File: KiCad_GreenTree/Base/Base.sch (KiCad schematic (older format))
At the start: 21 parts, among them Q1 BCX56, Q2 BCX56, Q3 BCX56, Q4 BCX56, SW1 SW_DPDT_x2, U1 NE555D, U2 NE555D, U3 74HC04

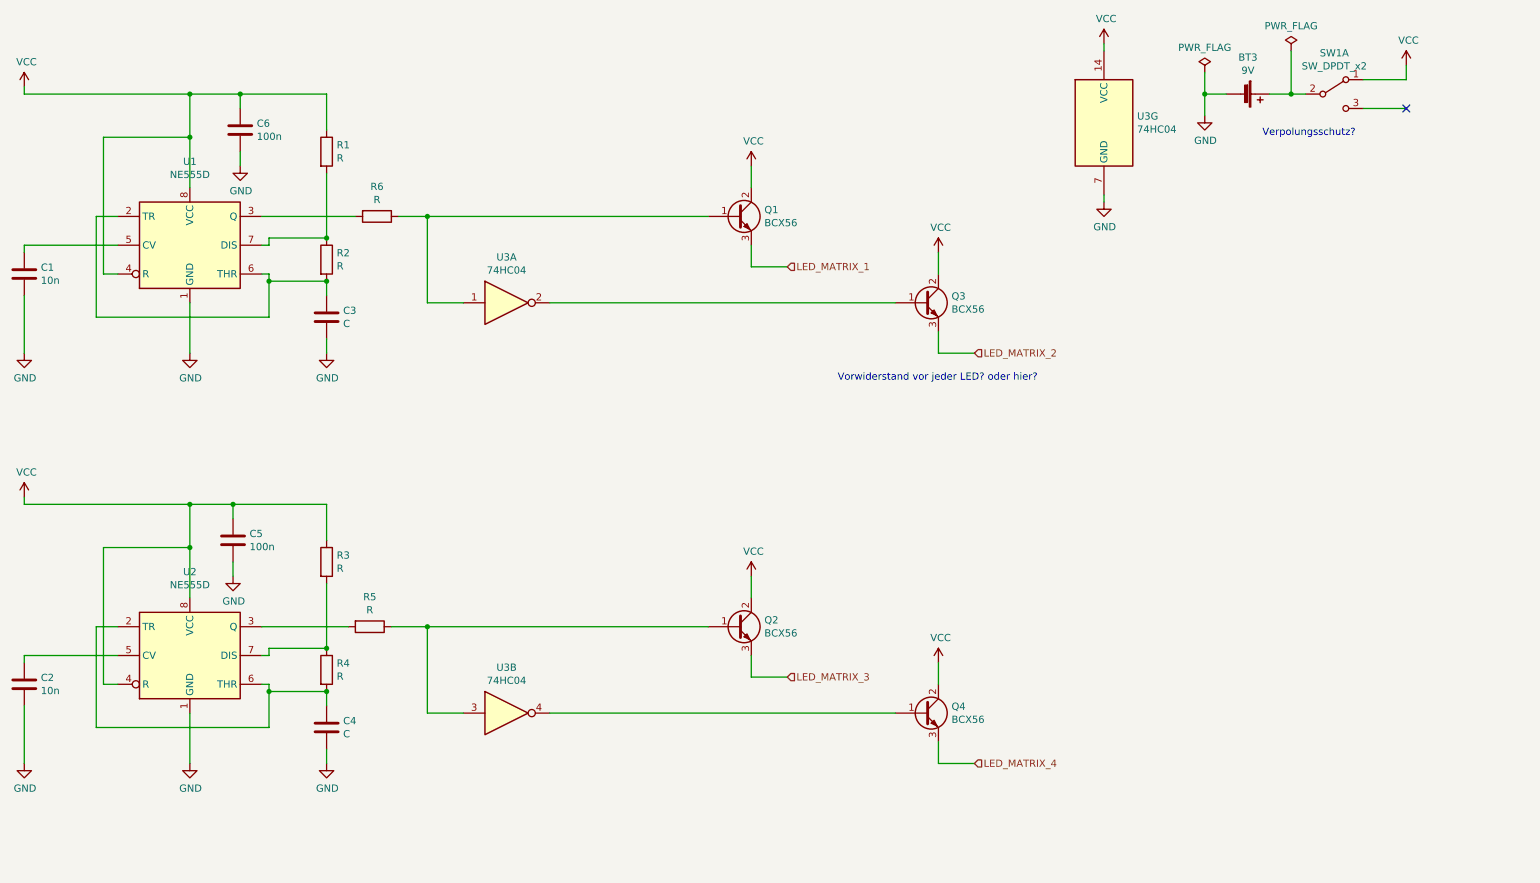
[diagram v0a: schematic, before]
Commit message: ordentlicher Schaltplan
NO DRC errors anymore
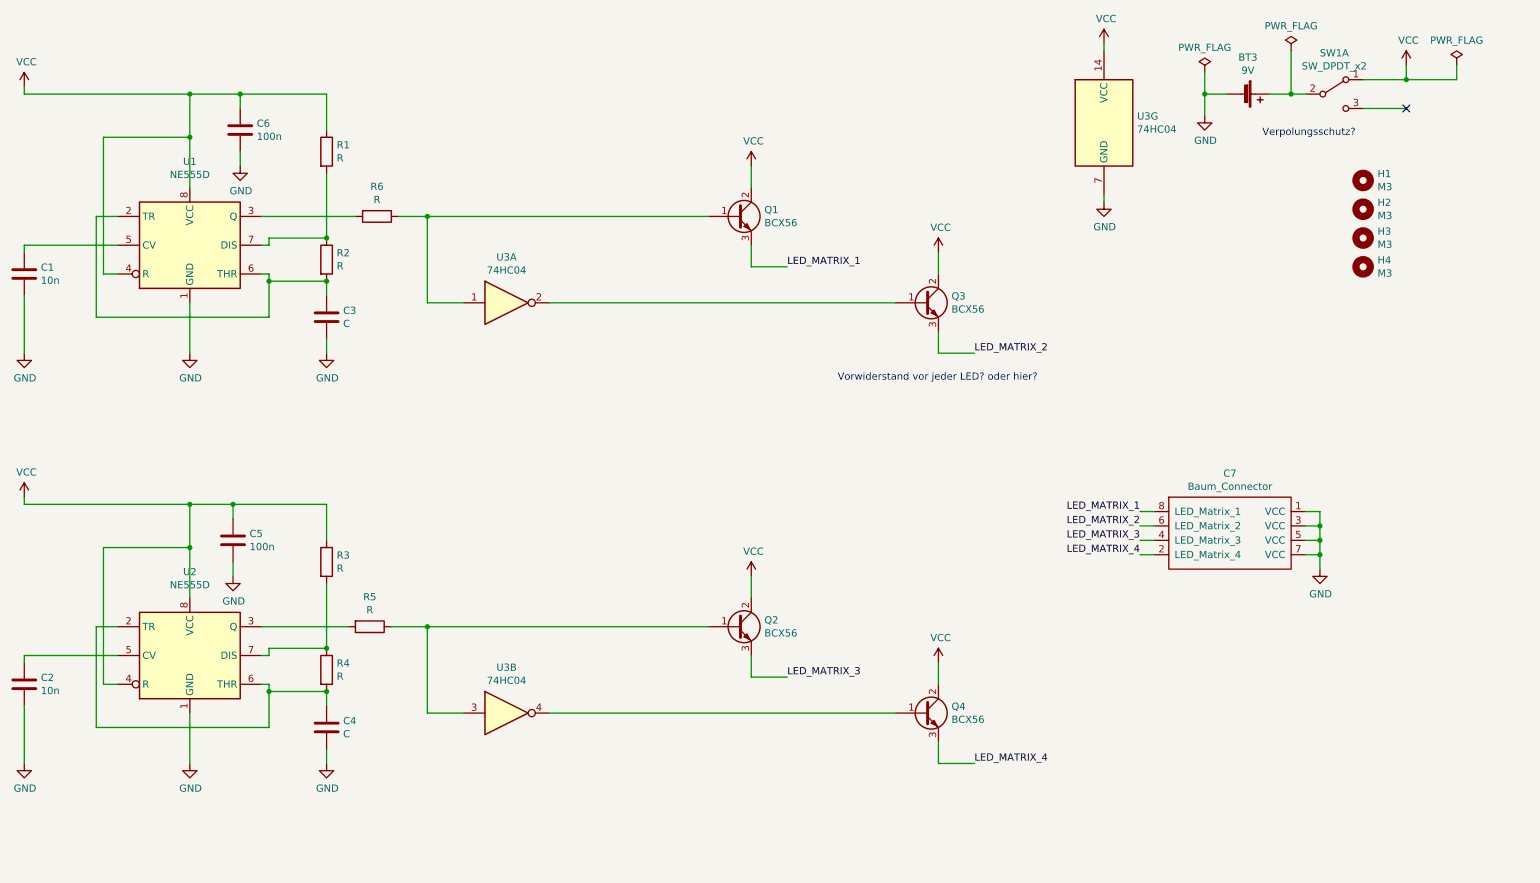
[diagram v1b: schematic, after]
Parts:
- added C7: Baum_Connector, Bib:Verbindung_Basis, symbol New_Library:Baum_Connector
- added H1, H2, H3, H4: M3, MountingHole:MountingHole_3.2mm_M3, symbol Mechanical:MountingHole
- U3: footprint (none) -> Package_SO:SOIC-14W_7.5x9mm_P1.27mm
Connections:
- net GND: now also C7.1 (VCC), C7.3 (VCC), C7.5 (VCC), C7.7 (VCC)
- net LED_MATRIX_1: now also C7.8 (LED_Matrix_1)
- net LED_MATRIX_2: now also C7.6 (LED_Matrix_2)
- net LED_MATRIX_3: now also C7.4 (LED_Matrix_3)
- net LED_MATRIX_4: now also C7.2 (LED_Matrix_4)
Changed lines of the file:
@@
 Wire Wire Line
 	2950 1050 2950 1300
-Connection ~ 2000 1050
 Wire Wire Line
 	2950 2450 2950 2350
@@
 $EndComp
 Wire Wire Line
-	850  1000 850  1050
-Wire Wire Line
 	1500 1900 1350 1900
 Wire Wire Line
@@
 	2550 2600 2550 2350
 Connection ~ 2550 2350
-Wire Wire Line
-	850  1050 2000 1050
 Wire Wire Line
 	1500 2300 1400 2300
@@
 Wire Wire Line
 	4500 5350 6900 5350
-Wire Wire Line
-	5900 2100 5900 2250
-Wire Wire Line
-	5900 2250 6150 2250
-Wire Wire Line
-	7200 2700 7200 2850
-Wire Wire Line
-	7200 2850 7450 2850
-Text HLabel 6150 2250 2    50   Input ~ 0
-LED_MATRIX_1
-Text HLabel 7450 2850 2    50   Input ~ 0
-LED_MATRIX_2
-Wire Wire Line
-	5900 4950 5900 5100
-Wire Wire Line
-	5900 5100 6150 5100
-Wire Wire Line
-	7200 5550 7200 5700
-Wire Wire Line
-	7200 5700 7450 5700
-Text HLabel 6150 5100 2    50   Input ~ 0
-LED_MATRIX_3
-Text HLabel 7450 5700 2    50   Input ~ 0
-LED_MATRIX_4
 $Comp
 L power:VCC #PWR0111
@@
 Wire Wire Line
 	3650 5350 3900 5350
-Wire Wire Line
-	10150 950  10450 950
 $Comp
 L power:VCC #PWR0109
@@
 	1    0    0    -1
 $EndComp
-Wire Wire Line
-	10450 950  10450 850
 NoConn ~ 10450 1150
 Wire Wire Line
@@
 F 0 "U3" H 8580 1296 50  0000 L CNN
 F 1 "74HC04" H 8580 1205 50  0000 L CNN
-F 2 "" H 8350 1250 50  0001 C CNN
+F 2 "Package_SO:SOIC-14W_7.5x9mm_P1.27mm" H 8350 1250 50  0001 C CNN
 F 3 "https://assets.nexperia.com/documents/data-sheet/74HC_HCT04.pdf" H 8350 1250 50  0001 C CNN
 	7    8350 1250
@@
 Wire Wire Line
 	8350 750  8350 700
+$Comp
+L Mechanical:MountingHole H1
+U 1 1 61701100
+P 10150 1650
+F 0 "H1" H 10250 1696 50  0000 L CNN
+F 1 "M3" H 10250 1605 50  0000 L CNN
+F 2 "MountingHole:MountingHole_3.2mm_M3" H 10150 1650 50  0001 C CNN
+F 3 "~" H 10150 1650 50  0001 C CNN
+	1    10150 1650
+	1    0    0    -1
+$EndComp
+$Comp
+L Mechanical:MountingHole H2
+U 1 1 6170B577
+P 10150 1850
+F 0 "H2" H 10250 1896 50  0000 L CNN
+F 1 "M3" H 10250 1805 50  0000 L CNN
+F 2 "MountingHole:MountingHole_3.2mm_M3" H 10150 1850 50  0001 C CNN
+F 3 "~" H 10150 1850 50  0001 C CNN
+	1    10150 1850
+	1    0    0    -1
+$EndComp
+$Comp
+L Mechanical:MountingHole H3
+U 1 1 6170D693
+P 10150 2050
+F 0 "H3" H 10250 2096 50  0000 L CNN
+F 1 "M3" H 10250 2005 50  0000 L CNN
+F 2 "MountingHole:MountingHole_3.2mm_M3" H 10150 2050 50  0001 C CNN
+F 3 "~" H 10150 2050 50  0001 C CNN
+	1    10150 2050
+	1    0    0    -1
+$EndComp
+$Comp
+L Mechanical:MountingHole H4
+U 1 1 6170F813
+P 10150 2250
+F 0 "H4" H 10250 2296 50  0000 L CNN
+F 1 "M3" H 10250 2205 50  0000 L CNN
+F 2 "MountingHole:MountingHole_3.2mm_M3" H 10150 2250 50  0001 C CNN
+F 3 "~" H 10150 2250 50  0001 C CNN
+	1    10150 2250
+	1    0    0    -1
+$EndComp
+Wire Wire Line
+	5900 4950 5900 5100
+Wire Wire Line
+	5900 5100 6150 5100
+Wire Wire Line
+	850  1000 850  1050
+Wire Wire Line
+	850  1050 2000 1050
+Connection ~ 2000 1050
+Wire Wire Line
+	7200 2700 7200 2850
+Wire Wire Line
+	7200 2850 7450 2850
+Wire Wire Line
+	10150 950  10450 950
+Wire Wire Line
+	10450 950  10450 850
+$Comp
+L power:PWR_FLAG #FLG0103
+U 1 1 61739FC1
+P 10800 850
+F 0 "#FLG0103" H 10800 925 50  0001 C CNN
+F 1 "PWR_FLAG" H 10800 1023 50  0000 C CNN
+F 2 "" H 10800 850 50  0001 C CNN
+F 3 "~" H 10800 850 50  0001 C CNN
+	1    10800 850
+	1    0    0    -1
+$EndComp
+Wire Wire Line
+	10450 950  10800 950
+Wire Wire Line
+	10800 950  10800 850
+Connection ~ 10450 950
+Wire Wire Line
+	5900 2250 6150 2250
+Wire Wire Line
+	7450 5700 7200 5700
+Wire Wire Line
+	7200 5700 7200 5550
+Text Label 7450 2850 0    50   ~ 0
+LED_MATRIX_2
+Text Label 6150 2250 0    50   ~ 0
+LED_MATRIX_1
+Text Label 6150 5100 0    50   ~ 0
+LED_MATRIX_3
+Text Label 7450 5700 0    50   ~ 0
+LED_MATRIX_4
+Wire Wire Line
+	5900 2250 5900 2100
+$Comp
+L New_Library:Baum_Connector C7
+U 1 1 6175B844
+P 8800 3850
+F 0 "C7" H 9225 4015 50  0000 C CNN
+F 1 "Baum_Connector" H 9225 3924 50  0000 C CNN
+F 2 "Bib:Verbindung_Basis" H 9200 3300 50  0001 C CNN
+F 3 "" H 9200 3300 50  0001 C CNN
+	1    8800 3850
+	1    0    0    -1
+$EndComp
+$Comp
+L power:GND #PWR0117
+U 1 1 6175CED1
+P 9850 4350
+F 0 "#PWR0117" H 9850 4100 50  0001 C CNN
+F 1 "GND" H 9855 4177 50  0000 C CNN
+F 2 "" H 9850 4350 50  0001 C CNN
+F 3 "" H 9850 4350 50  0001 C CNN
+	1    9850 4350
+	1    0    0    -1
+$EndComp
+Wire Wire Line
+	9850 4350 9850 4250
+Wire Wire Line
+	9850 4250 9750 4250
+Wire Wire Line
+	9850 4250 9850 4150
+Wire Wire Line
+	9850 4150 9750 4150
+Connection ~ 9850 4250
+Wire Wire Line
+	9850 4150 9850 4050
+Wire Wire Line
+	9850 4050 9750 4050
+Connection ~ 9850 4150
+Wire Wire Line
+	9850 4050 9850 3950
+Wire Wire Line
+	9850 3950 9750 3950
+Connection ~ 9850 4050
+Wire Wire Line
+	8700 3950 8600 3950
+Wire Wire Line
+	8700 4050 8600 4050
+Wire Wire Line
+	8700 4150 8600 4150
+Wire Wire Line
+	8700 4250 8600 4250
+Text Label 8600 3950 2    50   ~ 0
+LED_MATRIX_1
+Text Label 8600 4050 2    50   ~ 0
+LED_MATRIX_2
+Text Label 8600 4150 2    50   ~ 0
+LED_MATRIX_3
+Text Label 8600 4250 2    50   ~ 0
+LED_MATRIX_4
 $EndSCHEMATC

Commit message: Added Diodes
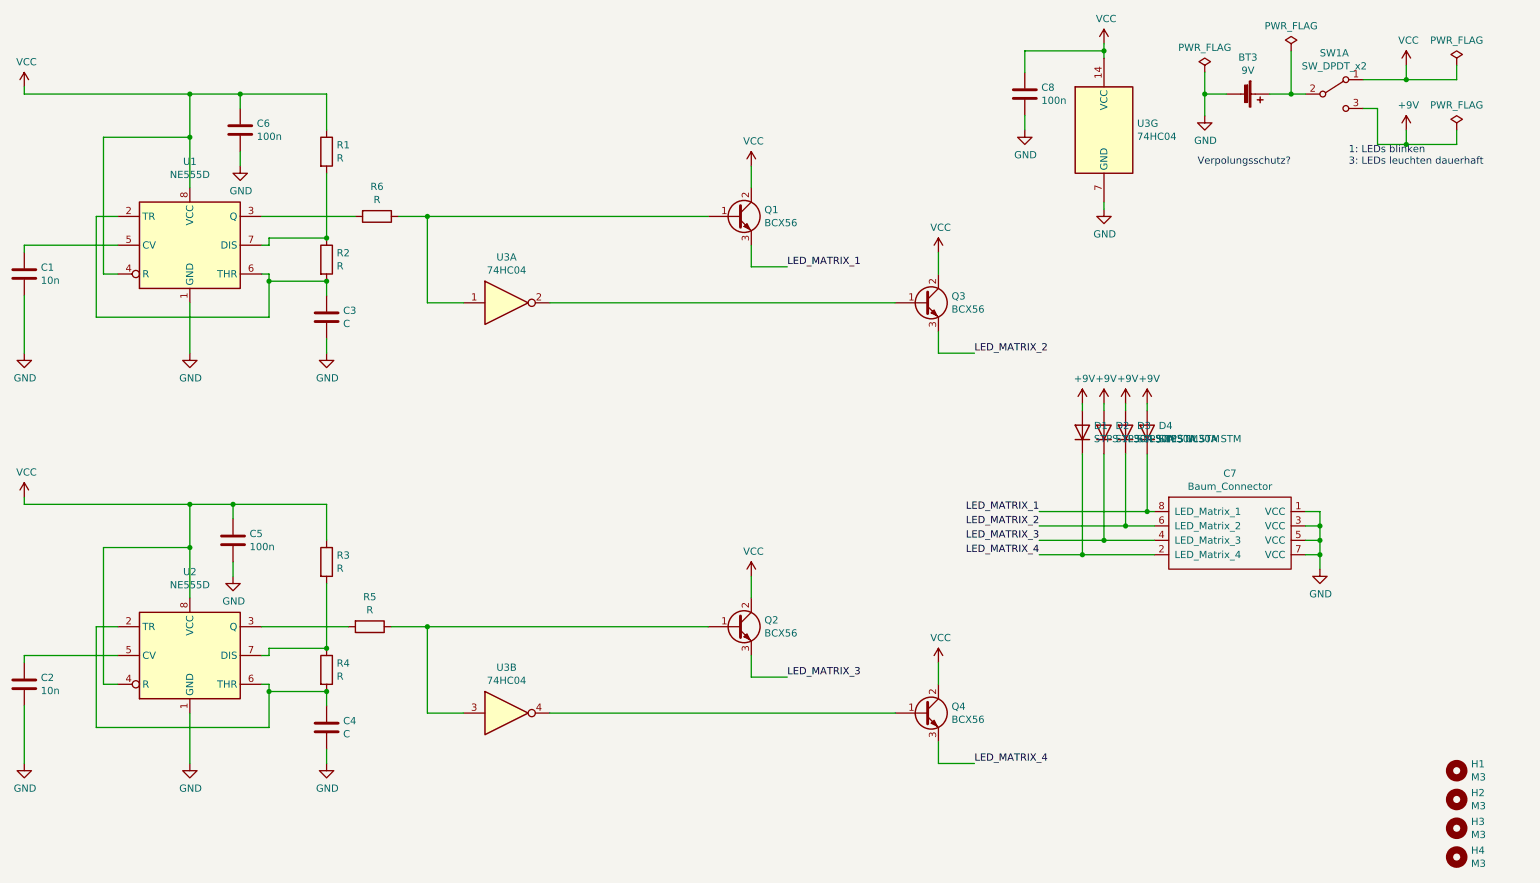
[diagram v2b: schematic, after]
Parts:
- added C8: 100n, Capacitor_SMD:C_1206_3216Metric_Pad1.33x1.80mm_HandSolder, symbol Device:C
- added D1, D2, D3, D4: STPS 1L30A STM, Diode_SMD:D_SMA_Handsoldering, symbol Device:D
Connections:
- net GND: now also C8.2
- net LED_MATRIX_1: now also D4.1 (K)
- net LED_MATRIX_2: now also D3.1 (K)
- net LED_MATRIX_3: now also D2.1 (K)
- net LED_MATRIX_4: now also D1.1 (K)
- net VCC: now also C8.1
- net +9V: now reaches SW1.3 (C)
- net +9V: now also D1.2 (A), D2.2 (A), D3.2 (A), D4.2 (A)
- no-connect marks 1 -> 0
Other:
- note added: "1: LEDs blinken\n3: LEDs leuchten dauerhaft\n"
- note removed: "Vorwiderstand vor jeder LED? oder hier?"
- moved on the sheet: H1, H2, H3, H4, U3G

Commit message: added 5V
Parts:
- added C10: 10n, Capacitor_SMD:C_1206_3216Metric_Pad1.33x1.80mm_HandSolder, symbol Device:C
- added C9: 330n, Capacitor_SMD:C_1206_3216Metric_Pad1.33x1.80mm_HandSolder, symbol Device:C
- added R7, R8: R, Resistor_SMD:R_1206_3216Metric_Pad1.30x1.75mm_HandSolder, symbol Device:R
- added U4: L78L05_TO92, Package_TO_SOT_THT:TO-92_Inline, symbol Regulator_Linear:L78L05_TO92
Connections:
- net GND: now also C10.2, C9.2, U4.2 (GND)
- net VCC: now also C9.1, U4.3 (VI); no longer C5.1, C6.1, C8.1, R1.1, R3.1, U1.4 (R), U1.8 (VCC), U2.4 (R), U2.8 (VCC), U3.14 (VCC)
- net at U3.4: now also R7.2; no longer Q4.1 (B)
- net at U3.2: now also R8.2; no longer Q3.1 (B)
- new net: Q3.1 (B), R8.1
- new net: Q4.1 (B), R7.1
- new net +5V: C10.1, C5.1, C6.1, C8.1, R1.1, R3.1, U1.4 (R), U1.8 (VCC), U2.4 (R), U2.8 (VCC), U3.14 (VCC), U4.1 (VO)
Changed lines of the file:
@@
 Wire Wire Line
 	2000 2850 2000 2500
-$Comp
-L power:VCC #PWR0103
-U 1 1 616CE65E
-P 850 1000
-F 0 "#PWR0103" H 850 850 50  0001 C CNN
-F 1 "VCC" H 865 1173 50  0000 C CNN
-F 2 "" H 850 1000 50  0001 C CNN
-F 3 "" H 850 1000 50  0001 C CNN
-	1    850  1000
-	1    0    0    -1
-$EndComp
 Wire Wire Line
 	1500 1900 1350 1900
@@
 Wire Wire Line
 	2000 5700 2000 5350
-$Comp
-L power:VCC #PWR0107
-U 1 1 616DFE58
-P 850 3850
-F 0 "#PWR0107" H 850 3700 50  0001 C CNN
-F 1 "VCC" H 865 4023 50  0000 C CNN
-F 2 "" H 850 3850 50  0001 C CNN
-F 3 "" H 850 3850 50  0001 C CNN
-	1    850  3850
-	1    0    0    -1
-$EndComp
 Wire Wire Line
 	850  3850 850  3900
@@
 	3650 1900 5600 1900
 Wire Wire Line
-	4500 2500 6900 2500
-Wire Wire Line
 	2500 4750 3100 4750
 Wire Wire Line
@@
 Wire Wire Line
 	3650 4750 5600 4750
-Wire Wire Line
-	4500 5350 6900 5350
 $Comp
 L power:VCC #PWR0111
@@
 F 3 "https://assets.nexperia.com/documents/data-sheet/74HC_HCT04.pdf" H 8350 1300 50  0001 C CNN
 	7    8350 1300
-	1    0    0    -1
-$EndComp
-$Comp
-L power:VCC #PWR0115
-U 1 1 61712EF3
-P 8350 700
-F 0 "#PWR0115" H 8350 550 50  0001 C CNN
-F 1 "VCC" H 8365 873 50  0000 C CNN
-F 2 "" H 8350 700 50  0001 C CNN
-F 3 "" H 8350 700 50  0001 C CNN
-	1    8350 700
 	1    0    0    -1
 $EndComp
@@
 	0    -1   -1   0
 $EndComp
+$Comp
+L Regulator_Linear:L78L05_TO92 U4
+U 1 1 618CD78C
+P 10000 2200
+F 0 "U4" H 10000 2442 50  0000 C CNN
+F 1 "L78L05_TO92" H 10000 2351 50  0000 C CNN
+F 2 "Package_TO_SOT_THT:TO-92_Inline" H 10000 2425 50  0001 C CIN
+F 3 "http://www.st.com/content/ccc/resource/technical/document/datasheet/15/55/e5/aa/23/5b/43/fd/CD00000446.pdf/files/CD00000446.pdf/jcr:content/translations/en.CD00000446.pdf" H 10000 2150 50  0001 C CNN
+	1    10000 2200
+	1    0    0    -1
+$EndComp
+$Comp
+L power:VCC #PWR03
+U 1 1 618D44C5
+P 9300 2150
+F 0 "#PWR03" H 9300 2000 50  0001 C CNN
+F 1 "VCC" H 9315 2323 50  0000 C CNN
+F 2 "" H 9300 2150 50  0001 C CNN
+F 3 "" H 9300 2150 50  0001 C CNN
+	1    9300 2150
+	1    0    0    -1
+$EndComp
+$Comp
+L power:+5V #PWR07
+U 1 1 618D865F
+P 10850 2100
+F 0 "#PWR07" H 10850 1950 50  0001 C CNN
+F 1 "+5V" H 10865 2273 50  0000 C CNN
+F 2 "" H 10850 2100 50  0001 C CNN
+F 3 "" H 10850 2100 50  0001 C CNN
+	1    10850 2100
+	1    0    0    -1
+$EndComp
+$Comp
+L power:GND #PWR06
+U 1 1 618D9458
+P 10550 2650
+F 0 "#PWR06" H 10550 2400 50  0001 C CNN
+F 1 "GND" H 10555 2477 50  0000 C CNN
+F 2 "" H 10550 2650 50  0001 C CNN
+F 3 "" H 10550 2650 50  0001 C CNN
+	1    10550 2650
+	1    0    0    -1
+$EndComp
+$Comp
+L power:GND #PWR04
+U 1 1 618DA13F
+P 9500 2650
+F 0 "#PWR04" H 9500 2400 50  0001 C CNN
+F 1 "GND" H 9505 2477 50  0000 C CNN
+F 2 "" H 9500 2650 50  0001 C CNN
+F 3 "" H 9500 2650 50  0001 C CNN
+	1    9500 2650
+	1    0    0    -1
+$EndComp
+$Comp
+L power:GND #PWR05
+U 1 1 618DE08D
+P 10000 2650
+F 0 "#PWR05" H 10000 2400 50  0001 C CNN
+F 1 "GND" H 10005 2477 50  0000 C CNN
+F 2 "" H 10000 2650 50  0001 C CNN
+F 3 "" H 10000 2650 50  0001 C CNN
+	1    10000 2650
+	1    0    0    -1
+$EndComp
+$Comp
+L Device:C C9
+U 1 1 618E27A2
+P 9500 2400
+F 0 "C9" H 9615 2446 50  0000 L CNN
+F 1 "330n" H 9615 2355 50  0000 L CNN
+F 2 "Capacitor_SMD:C_1206_3216Metric_Pad1.33x1.80mm_HandSolder" H 9538 2250 50  0001 C CNN
+F 3 "~" H 9500 2400 50  0001 C CNN
+	1    9500 2400
+	1    0    0    -1
+$EndComp
+$Comp
+L Device:C C10
+U 1 1 618E31F1
+P 10550 2400
+F 0 "C10" H 10665 2446 50  0000 L CNN
+F 1 "10n" H 10665 2355 50  0000 L CNN
+F 2 "Capacitor_SMD:C_1206_3216Metric_Pad1.33x1.80mm_HandSolder" H 10588 2250 50  0001 C CNN
+F 3 "~" H 10550 2400 50  0001 C CNN
+	1    10550 2400
+	1    0    0    -1
+$EndComp
+Wire Wire Line
+	9300 2150 9300 2200
+Wire Wire Line
+	10300 2200 10550 2200
+Wire Wire Line
+	10850 2200 10850 2100
+Wire Wire Line
+	10550 2200 10550 2250
+Connection ~ 10550 2200
+Wire Wire Line
+	10550 2200 10850 2200
+Wire Wire Line
+	10550 2550 10550 2650
+Wire Wire Line
+	10000 2500 10000 2650
+Wire Wire Line
+	9500 2250 9500 2200
+Wire Wire Line
+	9300 2200 9500 2200
+Connection ~ 9500 2200
+Wire Wire Line
+	9500 2200 9700 2200
+Wire Wire Line
+	9500 2650 9500 2550
+$Comp
+L Device:R R8
+U 1 1 6192C9D4
+P 5450 2500
+F 0 "R8" V 5243 2500 50  0000 C CNN
+F 1 "R" V 5334 2500 50  0000 C CNN
+F 2 "Resistor_SMD:R_1206_3216Metric_Pad1.30x1.75mm_HandSolder" V 5380 2500 50  0001 C CNN
+F 3 "~" H 5450 2500 50  0001 C CNN
+	1    5450 2500
+	0    1    1    0
+$EndComp
+Wire Wire Line
+	4500 2500 5300 2500
+Wire Wire Line
+	5600 2500 6900 2500
+$Comp
+L Device:R R7
+U 1 1 619441AF
+P 5350 5350
+F 0 "R7" V 5143 5350 50  0000 C CNN
+F 1 "R" V 5234 5350 50  0000 C CNN
+F 2 "Resistor_SMD:R_1206_3216Metric_Pad1.30x1.75mm_HandSolder" V 5280 5350 50  0001 C CNN
+F 3 "~" H 5350 5350 50  0001 C CNN
+	1    5350 5350
+	0    1    1    0
+$EndComp
+Wire Wire Line
+	4500 5350 5200 5350
+Wire Wire Line
+	5500 5350 6900 5350
+$Comp
+L power:+5V #PWR0103
+U 1 1 61965175
+P 8350 700
+F 0 "#PWR0103" H 8350 550 50  0001 C CNN
+F 1 "+5V" H 8365 873 50  0000 C CNN
+F 2 "" H 8350 700 50  0001 C CNN
+F 3 "" H 8350 700 50  0001 C CNN
+	1    8350 700
+	1    0    0    -1
+$EndComp
+$Comp
+L power:+5V #PWR0107
+U 1 1 61969B0B
+P 850 1000
+F 0 "#PWR0107" H 850 850 50  0001 C CNN
+F 1 "+5V" H 865 1173 50  0000 C CNN
+F 2 "" H 850 1000 50  0001 C CNN
+F 3 "" H 850 1000 50  0001 C CNN
+	1    850  1000
+	1    0    0    -1
+$EndComp
+$Comp
+L power:+5V #PWR0115
+U 1 1 6196E45E
+P 850 3850
+F 0 "#PWR0115" H 850 3700 50  0001 C CNN
+F 1 "+5V" H 865 4023 50  0000 C CNN
+F 2 "" H 850 3850 50  0001 C CNN
+F 3 "" H 850 3850 50  0001 C CNN
+	1    850  3850
+	1    0    0    -1
+$EndComp
 $EndSCHEMATC

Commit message: fixed Inv
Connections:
- net LED_MATRIX_2: now also Q2.3 (E); no longer Q3.3 (E)
- net LED_MATRIX_3: now also Q3.3 (E); no longer Q2.3 (E)
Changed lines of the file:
@@
 Wire Wire Line
 	7200 5700 7200 5550
-Text Label 7450 2850 0    50   ~ 0
+Text Label 6150 5100 0    50   ~ 0
 LED_MATRIX_2
 Text Label 6150 2250 0    50   ~ 0
 LED_MATRIX_1
-Text Label 6150 5100 0    50   ~ 0
+Text Label 7450 2850 0    50   ~ 0
 LED_MATRIX_3
 Text Label 7450 5700 0    50   ~ 0
